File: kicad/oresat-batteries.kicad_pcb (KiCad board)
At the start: 4 copper layers, 99.8 x 94.6 mm, 309 parts, among them J1 J-SAMTEC-TFM-120-X1-XXX-D-RA, J2 FTS-102-01-X-SJ, J4 ORESAT-DEBUG-CONNECTOR-ALL, Q1 DMP2240UDM, Q12 Si7625DN, Q13 Si7625DN, Q14 NTR4101, Q15 NTR4101, Q16 Si7625DN, Q17 Si7625DN, Q18 Si7625DN, Q19 Si7625DN, Q2 PMV45EN, Q20 PMV45EN, Q21 PMV45EN, Q24 PM45VEN, Q25 PM45VEN, Q26 PM45VEN, Q27 PM45VEN, Q3 DMP3050LVT-7, Q30 Si7625DN, Q31 Si7625DN, Q32 NTR4101, Q33 NTR4101, Q34 Si7625DN, Q35 Si7625DN, Q36 Si7625DN, Q37 Si7625DN, Q38 PMV45EN, Q39 PMV45EN, Q4 DMP3050LVT-7, Q42 DMP2240UDM, Q43 DMP2240UDM, Q44 PMV45EN, Q5 PMV45EN, Q6 PM45VEN, Q7 PM45VEN, Q8 PM45VEN, Q9 PM45VEN, SW1 OMRON-D2F-5L3-LEFT, SW2 OMRON-D2F-5L3-RIGHT, SW3 OMRON-D2F-5L3-LEFT, SW4 OMRON-D2F-5L3-RIGHT, U1 MAX7310ATE, U10 LTC4412, U11 LTC4412, U12 MAX17205G, U13 S-8209AAA-T8T1U, U14 S-8209AAA-T8T1U, U15 LTC4412, U16 LTC4412, U17 MAX17205G, U2 MIC842LYC5, U20 TCAN330, U21 STM32F091C, U3 MIC842LYC5, U4 MAX4211FETE, U5 TPS62111RSA, U6 TS5A21366DCUR, U8 S-8209AAA-T8T1U, U9 S-8209AAA-T8T1U, X3 16MHZ-2.5x2mm

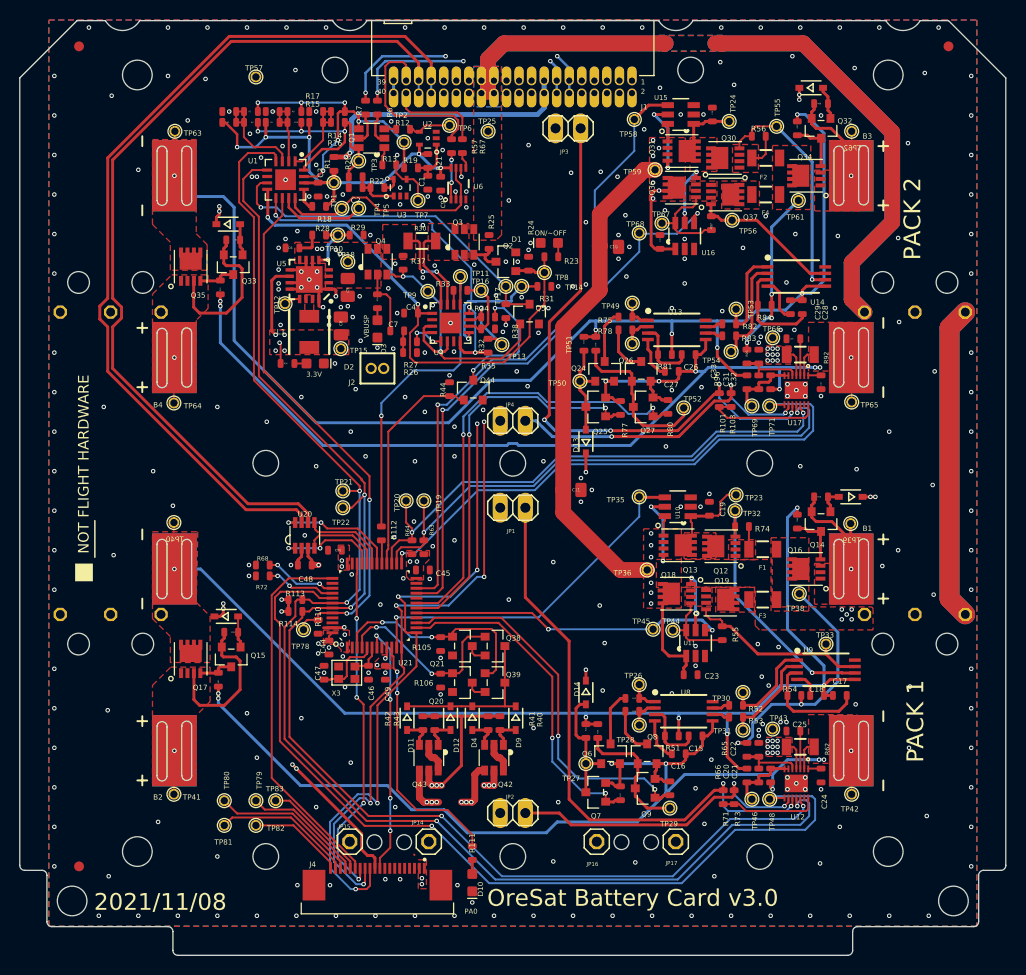
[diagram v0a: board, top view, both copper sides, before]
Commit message: Updating KiCAD import of EAGLE battery card v3.0 and calling it v3.1 because the gerber files will definitely be different and we'll probably implement a few small changes. Reimports, renames, and fixes .gitignore file. Oh and makes the worksheets pretty.
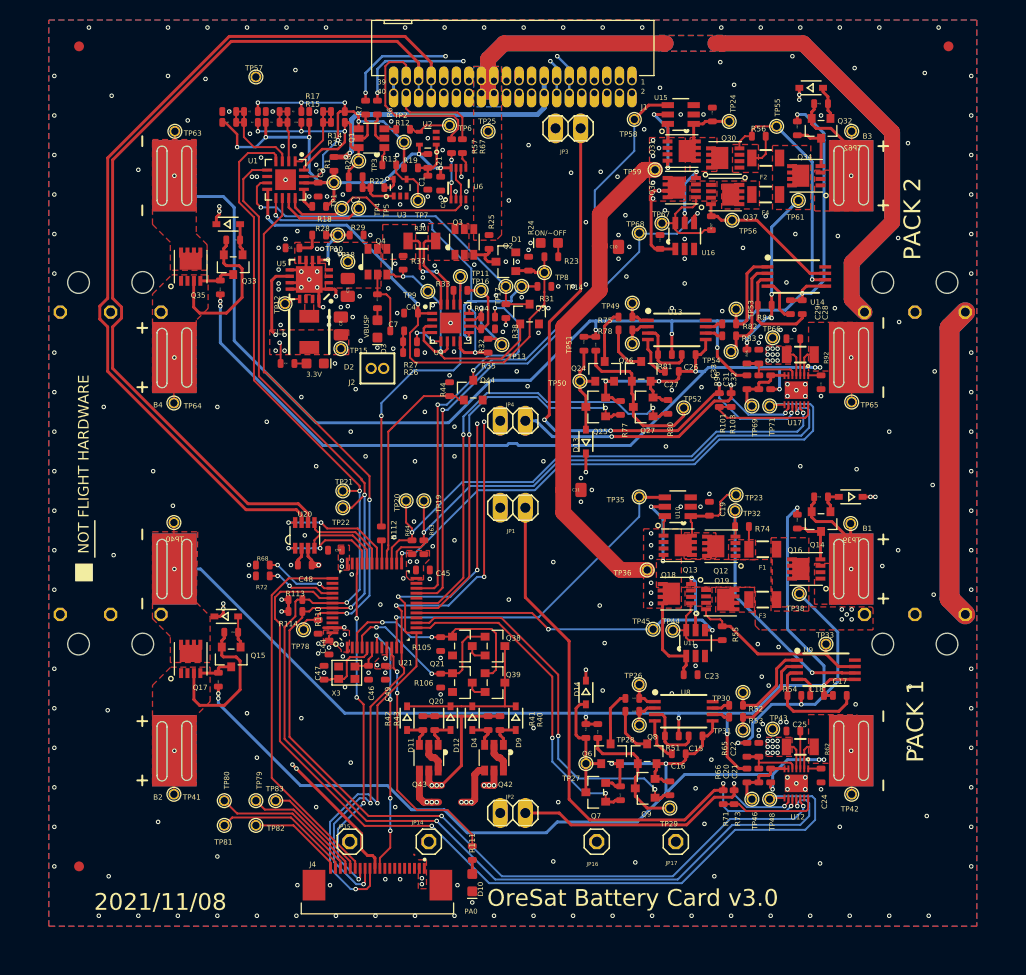
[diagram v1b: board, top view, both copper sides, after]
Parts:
- removed U$2: , oresat-batteries:ORESAT-CARD-V1.3-BATTERY-V3.0
- F1, F2: value 1206L500/12SLPR -> GENERIC-FUSE-1206
- F3, F4: value 1206L150/12SLYR -> GENERIC-FUSE-1206
- J2: value FTS-102-01-X-SJ -> SAMTEC-FTS-102-01-X-SJ
- JP1, JP2, JP3, JP4: value (none) -> PINHD-1X2
- JP14, JP15, JP16, JP17: value (none) -> PINHD-1X1
- Q1, Q42, Q43: value DMP2240UDM -> MOSFET-PCH-SOT23-6
- Q12, Q13, Q16, Q17, Q18, Q19, Q30, Q31, Q34, Q35, Q36, Q37: value Si7625DN -> Q-VISHAY-MOSFET-PCH-POWERPAK-1212-8
- Q3, Q4: value DMP3050LVT-7 -> MOSFET-PCH-SOT23-6
- SW1, SW3: value OMRON-D2F-5L3-LEFT -> OMRON-D2F-L3-D-LEFT
- SW2, SW4: value OMRON-D2F-5L3-RIGHT -> OMRON-D2F-L3-D-RIGHT
- U1: value MAX7310ATE -> MAX7310
- U13, U14, U8, U9: value S-8209AAA-T8T1U -> S-8209AXXT
- U4: value MAX4211FETE -> MAX4211
- U5: value TPS62111RSA -> TPS6211X
- X3: value 16MHZ-2.5x2mm -> CRYSTAL-WITH-GND
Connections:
- net AD0 renamed /Power/AD0
- net AD1 renamed /Power/AD1
- net AD2 renamed /Power/AD2
- net AIN1-PK1 renamed Net-(U12-AIN1)
- net AIN1-PK2 renamed Net-(U17-AIN1)
- net AIN2-PK1 renamed Net-(U12-AIN2)
- net AIN2-PK2 renamed Net-(U17-AIN2)
- net CAN_RX renamed /Microcontroller/CAN_RX
- net CAN_SHDN renamed /Microcontroller/CAN_SHDN
- net CAN_TX renamed /Microcontroller/CAN_TX
- net CB-RESET renamed /Power/CB-RESET
- net CB_CTRL renamed /Power/CB_CTRL
- net CELL1-PK1 renamed Net-(U12-CELL1)
- net CELL1-PK2 renamed Net-(U17-CELL1)
- net CRYSTALIN2 renamed Net-(U21-PF0-OSC_IN)
- net CRYSTALOUT2 renamed Net-(U21-PF1-OSC_OUT)
- net CSP-PK1 renamed /Battery Pack 1 (BOTTOM)/CSP-PK1
- net CSP-PK2 renamed /Battery Pack 2 (TOP)/CSP-PK2
- net HEATER renamed Net-(Q42B-D)
- net HEATER-ON-1 renamed /Microcontroller/HEATER-ON-1
- net HEATER-ON-2 renamed /Microcontroller/HEATER-ON-2
- net INTERCELL-PK1 renamed /Battery Pack 1 (BOTTOM)/INTERCELL-PK1
- net INTERCELL-PK2 renamed /Battery Pack 2 (TOP)/INTERCELL-PK2
- net INTERSW renamed Net-(SW3-PadNC)
- net IOUT1 renamed Net-(U4-IOUT)
- net NRESET renamed /Microcontroller/NRESET
- net ON/~{OFF} renamed /Power/ON/~{OFF}
- net PA0 renamed /Microcontroller/PA0
- net PA2/USART2_TX renamed PA2/USART2_TX
- net PA3/USART2_RX renamed PA3/USART2_RX
- net PA8/POUTPROT renamed /Microcontroller/PA8/POUTPROT
- net PA9/CAN_SILENT renamed /Microcontroller/PA9/CAN_SILENT
- net PB6/SCL renamed PB6/SCL
- net PB7/SDA renamed PB7/SDA
- net PEN-SCL-FILT renamed /Power/PEN-SCL-FILT
- net PEN-SDA-FILT renamed /Power/PEN-SDA-FILT
- net REG2-PK1 renamed Net-(U12-REG2)
- net REG2-PK2 renamed Net-(U17-REG2)
- net REG3-PK1 renamed Net-(U12-REG3)
- net REG3-PK2 renamed Net-(U17-REG3)
- net SWCLK renamed /Microcontroller/SWCLK
- net SWDIO renamed /Microcontroller/SWDIO
- net THRM-PK1 renamed Net-(U12-THRM)
- net THRM-PK2 renamed Net-(U17-THRM)
- net TPS62111-PG1 renamed Net-(U5-PG)
- net TPS62111-SYNC1 renamed Net-(U5-SYNC)
- net TPS62111_SW1 renamed Net-(L1-Pad1)
- net VBATT-F-PK1 renamed Net-(U10-VIN)
- net VBATT-F-PK2 renamed Net-(U15-VIN)
- net VBATT-PK1 renamed /Battery Pack 1 (BOTTOM)/VBATT-PK1
- net VBATT-PK2 renamed /Battery Pack 2 (TOP)/VBATT-PK2
- net VBATT-PL1 renamed Net-(U12-VBATT)
- net VBATT-PL2 renamed Net-(U17-VBATT)
- net ~{CHARGE-PK1} renamed /Battery Pack 1 (BOTTOM)/~{CHARGE-PK1}
- net ~{CHARGE-PK2} renamed /Battery Pack 2 (TOP)/~{CHARGE-PK2}
- net ~{DISCHARGE-PK1} renamed /Battery Pack 1 (BOTTOM)/~{DISCHARGE-PK1}
- net ~{DISCHARGE-PK2} renamed /Battery Pack 2 (TOP)/~{DISCHARGE-PK2}
- net ~{FAULT} renamed /Power/~{FAULT}
- FIDUCIAL1 pad FIDUCIAL: (no net) -> unconnected-(FIDUCIAL1-PadFIDUCIAL)
- FIDUCIAL2 pad FIDUCIAL: (no net) -> unconnected-(FIDUCIAL2-PadFIDUCIAL)
- FIDUCIAL3 pad FIDUCIAL: (no net) -> unconnected-(FIDUCIAL3-PadFIDUCIAL)
- J1 pad 1: (no net) -> unconnected-(J1-Pad1)
- J1 pad 10: (no net) -> unconnected-(J1-Pad10)
- J1 pad 17: (no net) -> unconnected-(J1-Pad17)
- J1 pad 18: (no net) -> unconnected-(J1-Pad18)
- J1 pad 19: (no net) -> unconnected-(J1-Pad19)
- J1 pad 2: (no net) -> unconnected-(J1-Pad2)
- J1 pad 20: (no net) -> unconnected-(J1-Pad20)
- J1 pad 21: (no net) -> unconnected-(J1-Pad21)
- J1 pad 22: (no net) -> unconnected-(J1-Pad22)
- J1 pad 3: (no net) -> unconnected-(J1-Pad3)
- J1 pad 31: (no net) -> unconnected-(J1-Pad31)
- J1 pad 32: (no net) -> unconnected-(J1-Pad32)
- J1 pad 4: (no net) -> unconnected-(J1-Pad4)
- J1 pad 5: (no net) -> unconnected-(J1-Pad5)
- J1 pad 6: (no net) -> unconnected-(J1-Pad6)
- J1 pad 7: (no net) -> unconnected-(J1-Pad7)
- J1 pad 8: (no net) -> unconnected-(J1-Pad8)
- J1 pad 9: (no net) -> unconnected-(J1-Pad9)
- J4 pad 4: (no net) -> unconnected-(J4-DEVICE-D+-Pad4)
- J4 pad 5: (no net) -> unconnected-(J4-DEVICE-D--Pad5)
- J4 pad 7: (no net) -> unconnected-(J4-HOST-D+-Pad7)
- J4 pad 8: (no net) -> unconnected-(J4-HOST-D--Pad8)
- Q31 pad 4: N$74 -> DCHG-STAT-OC-PK2
- SW1 pad NC: (no net) -> unconnected-(SW1-PadNC)
- SW2 pad NC: (no net) -> unconnected-(SW2-PadNC)
- SW3 pad NO: (no net) -> unconnected-(SW3-PadNO)
- SW4 pad NO: (no net) -> unconnected-(SW4-PadNO)
- U12 pad 13: (no net) -> unconnected-(U12-CELLX-Pad13)
- U13 pad 8: (no net) -> unconnected-(U13-CB-Pad8)
- U14 pad 8: (no net) -> unconnected-(U14-CB-Pad8)
- U15 pad 5: N$74 -> DCHG-STAT-OC-PK2
- U17 pad 13: (no net) -> unconnected-(U17-CELLX-Pad13)
- U21 pad 16: (no net) -> unconnected-(U21-PA6-Pad16)
- U21 pad 2: (no net) -> unconnected-(U21-PC13-Pad2)
- U21 pad 20: (no net) -> unconnected-(U21-PB2-Pad20)
- U21 pad 38: (no net) -> unconnected-(U21-PA15-Pad38)
- U21 pad 45: (no net) -> unconnected-(U21-PB8-Pad45)
- U21 pad 46: (no net) -> unconnected-(U21-PB9-Pad46)
- U8 pad 8: (no net) -> unconnected-(U8-CB-Pad8)
- U9 pad 8: (no net) -> unconnected-(U9-CB-Pad8)
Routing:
- net DCHG-STAT-OC-PK2: track 64.2 -> 72.3 mm, vias 1 -> 3
- net N$74: track 8.11 -> 0.00 mm, vias 2 -> 0
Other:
- board size 99.8 x 94.6 mm -> 72 x 6.1 mm

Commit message: Kicad import try #3. Now with DXFs from custom EAGLE layers. Schematic worksheets and names updated.
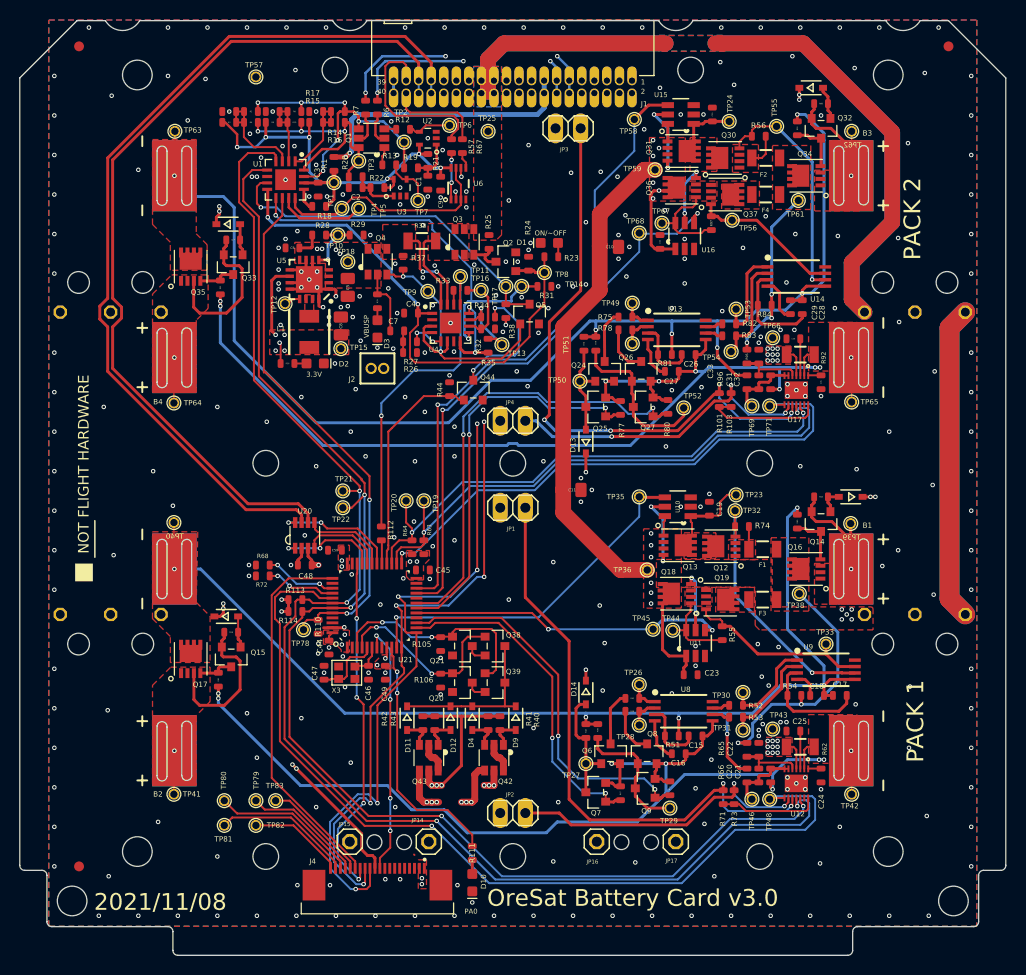
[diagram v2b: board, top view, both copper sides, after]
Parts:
- added U$2: , oresat-batteries:ORESAT-CARD-V1.3-BATTERY-V3.0, F.Cu at (98.6, 152.3)
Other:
- board size 72 x 6.1 mm -> 99.8 x 94.6 mm
